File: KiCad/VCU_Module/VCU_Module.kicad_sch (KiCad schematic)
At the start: 5 parts, among them J1 5810132011, J5 pin header, J7 5V, J8 3V3, J9 GND

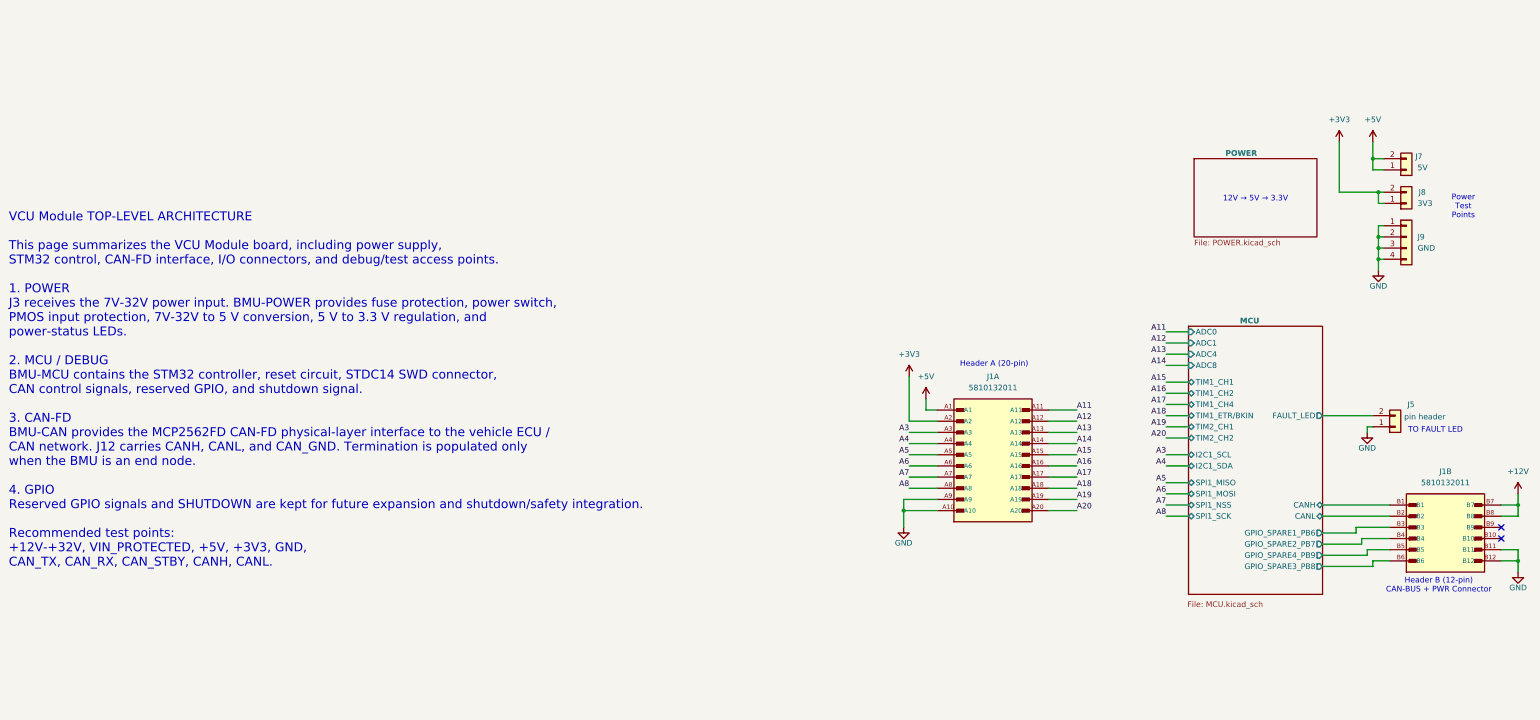
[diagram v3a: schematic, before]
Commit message: adding 'devkit' headers to make connections sustomizable inside of the enclosure
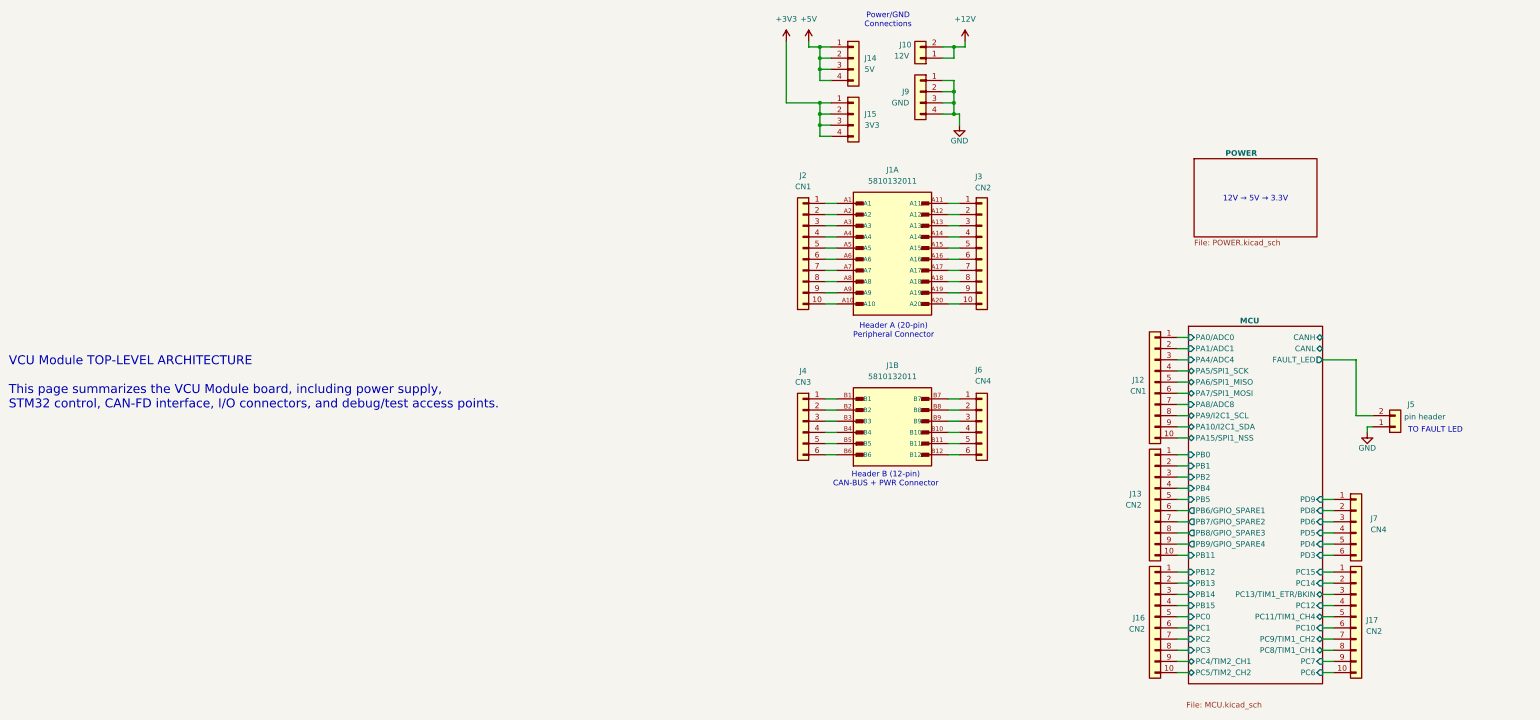
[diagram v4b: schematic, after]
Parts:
- removed J7: 5V, Connector_PinHeader_2.54mm:PinHeader_1x02_P2.54mm_Vertical, symbol Connector_Generic:Conn_01x02
- removed J8: 3V3, Connector_PinHeader_2.54mm:PinHeader_1x02_P2.54mm_Vertical, symbol Connector_Generic:Conn_01x02
- added J10: 12V, Connector_PinHeader_2.54mm:PinHeader_1x02_P2.54mm_Vertical, symbol Connector_Generic:Conn_01x02
- added J12, J2: CN1, symbol Connector_Generic:Conn_01x10
- added J13, J16, J17, J3: CN2, symbol Connector_Generic:Conn_01x10
- added J14: 5V, Connector_PinHeader_2.54mm:PinHeader_1x04_P2.54mm_Vertical, symbol Connector_Generic:Conn_01x04
- added J15: 3V3, Connector_PinHeader_2.54mm:PinHeader_1x04_P2.54mm_Vertical, symbol Connector_Generic:Conn_01x04
- added J4: CN3, symbol Connector_Generic:Conn_01x06
- added J6, J7: CN4, symbol Connector_Generic:Conn_01x06
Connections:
- net +12V: now also J10.1 (Pin_1), J10.2 (Pin_2); no longer J1.B7, J1.B8
- net +3V3: now also J15.1 (Pin_1), J15.2 (Pin_2), J15.3 (Pin_3), J15.4 (Pin_4); no longer J1.A2
- net +5V: now also J14.1 (Pin_1), J14.2 (Pin_2), J14.3 (Pin_3), J14.4 (Pin_4); no longer J1.A1
- net GND: no longer J1.A10, J1.A9, J1.B11, J1.B12
- net MCU/CANH: no longer J1.B1
- net MCU/CANL: no longer J1.B2
- net at J1.B10: now also J6.4 (Pin_4)
- net at J1.B9: now also J6.3 (Pin_3)
- net A11: no longer names the net of J1.A11
- net A11: now also J3.1 (Pin_1)
- net A12: no longer names the net of J1.A12
- net A12: now also J3.2 (Pin_2)
- net A13: no longer names the net of J1.A13
- net A13: now also J3.3 (Pin_3)
- net A14: no longer names the net of J1.A14
- net A14: now also J3.4 (Pin_4)
- net A15: no longer names the net of J1.A15
- net A15: now also J3.5 (Pin_5)
- net A16: no longer names the net of J1.A16
- net A16: now also J3.6 (Pin_6)
- net A17: no longer names the net of J1.A17
- net A17: now also J3.7 (Pin_7)
- net A18: no longer names the net of J1.A18
- net A18: now also J3.8 (Pin_8)
- net A19: no longer names the net of J1.A19
- net A19: now also J3.9 (Pin_9)
- net A20: no longer names the net of J1.A20
- net A20: now also J3.10 (Pin_10)
- net A3: no longer names the net of J1.A3
- net A3: now also J2.3 (Pin_3)
- net A4: no longer names the net of J1.A4
- net A4: now also J2.4 (Pin_4)
- net A5: no longer names the net of J1.A5
- net A5: now also J2.5 (Pin_5)
- net A6: no longer names the net of J1.A6
- net A6: now also J2.6 (Pin_6)
- net A7: no longer names the net of J1.A7
- net A7: now also J2.7 (Pin_7)
- net A8: no longer names the net of J1.A8
- net A8: now also J2.8 (Pin_8)
- net MCU/GPIO_SPARE1_PB6: no longer names the net of J1.B3
- net MCU/GPIO_SPARE1_PB6: now also J4.3 (Pin_3)
- net MCU/GPIO_SPARE2_PB7: no longer names the net of J1.B4
- net MCU/GPIO_SPARE2_PB7: now also J4.4 (Pin_4)
- net MCU/GPIO_SPARE3_PB8: no longer names the net of J1.B6
- net MCU/GPIO_SPARE3_PB8: now also J4.6 (Pin_6)
- net MCU/GPIO_SPARE4_PB9: no longer names the net of J1.B5
- net MCU/GPIO_SPARE4_PB9: now also J4.5 (Pin_5)
- new net: J1.B7, J6.1 (Pin_1)
- new net: J1.B8, J6.2 (Pin_2)
- new net: J1.B11, J6.5 (Pin_5)
- new net: J1.B12, J6.6 (Pin_6)
- new net: J1.A1, J2.1 (Pin_1)
- new net: J1.A10, J2.10 (Pin_10)
- new net: J1.A2, J2.2 (Pin_2)
- new net: J1.A9, J2.9 (Pin_9)
- new net: J1.B1, J4.1 (Pin_1)
- new net: J1.B2, J4.2 (Pin_2)
- new net MCU/PA0/ADC0: J12.1 (Pin_1)
- new net MCU/PA10/I2C1_SDA: J12.9 (Pin_9)
- new net MCU/PA15/SPI1_NSS: J12.10 (Pin_10)
- new net MCU/PA1/ADC1: J12.2 (Pin_2)
- new net MCU/PA4/ADC4: J12.3 (Pin_3)
- new net MCU/PA5/SPI1_SCK: J12.4 (Pin_4)
- new net MCU/PA6/SPI1_MISO: J12.5 (Pin_5)
- new net MCU/PA7/SPI1_MOSI: J12.6 (Pin_6)
- new net MCU/PA8/ADC8: J12.7 (Pin_7)
- new net MCU/PA9/I2C1_SCL: J12.8 (Pin_8)
- new net MCU/PB0: J13.1 (Pin_1)
- new net MCU/PB1: J13.2 (Pin_2)
- new net MCU/PB11: J13.10 (Pin_10)
- new net MCU/PB12: J16.1 (Pin_1)
- new net MCU/PB13: J16.2 (Pin_2)
- new net MCU/PB14: J16.3 (Pin_3)
- new net MCU/PB15: J16.4 (Pin_4)
- new net MCU/PB2: J13.3 (Pin_3)
- new net MCU/PB4: J13.4 (Pin_4)
- new net MCU/PB5: J13.5 (Pin_5)
- new net MCU/PB6/GPIO_SPARE1: J13.6 (Pin_6)
- new net MCU/PB7/GPIO_SPARE2: J13.7 (Pin_7)
- new net MCU/PB8/GPIO_SPARE3: J13.8 (Pin_8)
- new net MCU/PB9/GPIO_SPARE4: J13.9 (Pin_9)
- new net MCU/PC0: J16.5 (Pin_5)
- new net MCU/PC1: J16.6 (Pin_6)
- new net MCU/PC10: J17.6 (Pin_6)
- new net MCU/PC11/TIM1_CH4: J17.5 (Pin_5)
- new net MCU/PC12: J17.4 (Pin_4)
- new net MCU/PC13/TIM1_ETR/BKIN: J17.3 (Pin_3)
- new net MCU/PC14: J17.2 (Pin_2)
- new net MCU/PC15: J17.1 (Pin_1)
- new net MCU/PC2: J16.7 (Pin_7)
- new net MCU/PC3: J16.8 (Pin_8)
- new net MCU/PC4/TIM2_CH1: J16.9 (Pin_9)
- new net MCU/PC5/TIM2_CH2: J16.10 (Pin_10)
- new net MCU/PC6: J17.10 (Pin_10)
- new net MCU/PC7: J17.9 (Pin_9)
- new net MCU/PC8/TIM1_CH1: J17.8 (Pin_8)
- new net MCU/PC9/TIM1_CH2: J17.7 (Pin_7)
- new net MCU/PD3: J7.6 (Pin_6)
- new net MCU/PD4: J7.5 (Pin_5)
- new net MCU/PD5: J7.4 (Pin_4)
- new net MCU/PD6: J7.3 (Pin_3)
- new net MCU/PD8: J7.2 (Pin_2)
- new net MCU/PD9: J7.1 (Pin_1)
- no-connect marks 2 -> 0
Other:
- sheet MCU ports: added PA0/ADC0, PA10/I2C1_SDA, PA15/SPI1_NSS, PA1/ADC1, PA4/ADC4, PA5/SPI1_SCK, PA6/SPI1_MISO, PA7/SPI1_MOSI, PA8/ADC8, PA9/I2C1_SCL, PB0, PB1, PB11, PB12, PB13, PB14, PB15, PB2, PB4, PB5, PB6/GPIO_SPARE1, PB7/GPIO_SPARE2, PB8/GPIO_SPARE3, PB9/GPIO_SPARE4, PC0, PC1, PC10, PC11/TIM1_CH4, PC12, PC13/TIM1_ETR/BKIN, PC14, PC15, PC2, PC3, PC4/TIM2_CH1, PC5/TIM2_CH2, PC6, PC7, PC8/TIM1_CH1, PC9/TIM1_CH2, PD3, PD4, PD5, PD6, PD8, PD9; removed ADC0, ADC1, ADC4, ADC8, GPIO_SPARE1_PB6, GPIO_SPARE2_PB7, GPIO_SPARE3_PB8, GPIO_SPARE4_PB9, I2C1_SCL, I2C1_SDA, SPI1_MISO, SPI1_MOSI, SPI1_NSS, SPI1_SCK, TIM1_CH1, TIM1_CH2, TIM1_CH4, TIM1_ETR/BKIN, TIM2_CH1, TIM2_CH2
- note added: "Header A (20-pin) Peripheral Connector"
- note added: "Power/GND Connections"
- note added: "VCU Module TOP-LEVEL ARCHITECTURE This page summarizes the VCU Module board, including power supply, STM32 control, CAN-FD interface, I/O connectors, and debug/test access points."
- note removed: "Header A (20-pin)"
- note removed: "Power Test Points"
- note removed: "VCU Module TOP-LEVEL ARCHITECTURE This page summarizes the VCU Module board, including power supply, STM32 control, CAN-FD interface, I/O connectors, and debug/test access points. 1. POWER J3 receives the 7V-32V power input. BMU-POWER provides fuse protection, power switch, PMOS input protection, 7V-32V to 5 V conversion, 5 V to 3.3 V regulation, and power-status LEDs. 2. MCU / DEBUG BMU-MCU cont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"
- moved on the sheet: J1A, J1B

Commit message: added new power supply components, new power supply circuitry needs finishing
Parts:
- added C1, C2, C3: 10u, Capacitor_SMD:C_0805_2012Metric, symbol Device:C_Small
- added C4: 220n, Capacitor_SMD:C_0805_2012Metric, symbol Device:C_Small
- added CR1: MMSZ5245B-7-F, VMS_Footprints:SOD123_DIO, symbol MMSZ5245B_7_F:MMSZ5245B-7-F
- added D1, D2: GRN, LED_SMD:LED_0805_2012Metric_Pad1.15x1.40mm_HandSolder, symbol Device:LED
- added F1: Fuse, Fuse:Fuse_1206_3216Metric, symbol Device:Fuse
- added Q1: AO3401A, Package_TO_SOT_SMD:SOT-23, symbol Transistor_FET:AO3401A
- added R1, R4, R5: 100k, Resistor_SMD:R_0805_2012Metric, symbol Device:R_Small_US
- added R2, R3: 1k, Resistor_SMD:R_0805_2012Metric, symbol Device:R_Small_US
- added S1: 100SP1T1B4M2QE, VMS_Footprints:SW_100SP1T1B4M2QE, symbol 100SP1T1B4M2QE:100SP1T1B4M2QE
- added TP10, TP11, TP7, TP8, TP9: TestPoint_Small, TestPoint:TestPoint_THTPad_D1.5mm_Drill0.7mm, symbol Connector:TestPoint_Square
- added U1: OKI-78SR-5_1.5-W36-C, Converter_DCDC:Converter_DCDC_Murata_OKI-78SR_Vertical, symbol Converter_DCDC:OKI-78SR-5_1.5-W36-C
- added U2: TLV75533PDBV, Package_TO_SOT_SMD:SOT-23-5, symbol Regulator_Linear:TLV75533PDBV
- added U3: LMR33640DDDA, Package_SO:Texas_HSOP-8-1EP_3.9x4.9mm_P1.27mm_ThermalVias, symbol Regulator_Switching:LMR33640DDDA
- added U4: FDC6301N, FDC6301N:SSOT-6, symbol FDC6301N:FDC6301N
- J12: value CN1 -> MCU1
- J13: value CN2 -> MCU2
- J16: value CN2 -> MCU3
- J17: value CN2 -> MCU4
- J7: value CN4 -> MCU5
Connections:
- net +12V: now also F1.2, TP7.1
- net +3V3: now also C2.1, R3.2, R5.2, TP11.1, U2.5 (OUT)
- net +5V: now also C1.1, R2.2, R4.2, TP10.1, U1.3 (OUT), U2.1 (IN), U2.3 (EN)
- net GND: now also C1.2, C2.2, C3.2, C4.2, D1.1 (K), D2.1 (K), R1.2, TP9.1, U1.2 (GND), U2.2 (GND), U3.1 (GND), U3.9 (GND), U4.2, U4.6
- new net: CR1.2, Q1.1 (G), R1.1
- new net: Q1.3 (D), S1.1
- new net: D2.2 (A), R3.1
- new net: D1.2 (A), R2.1
- new net: F1.1, S1.2
- new net PG_3V3: R5.1, U3.4 (PG), U4.3
- new net PG_5V: R4.1, U4.5
- new net VDD: C3.1, C4.1, U3.2 (VIN), U3.3 (EN)
- new net VIN_PROTECTED: CR1.1, Q1.2 (S), TP8.1, U1.1 (IN)
- no-connect marks 0 -> 1
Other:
- removed sheet POWER
- note added: "3.3V @ 500 mA LDO"
- note added: "3V3 Supply Input Range: 3.8V-36V Output Range: 1V-24V"
- note added: "5V @ 1.5 A SPS"
- note added: "D"
- note added: "Enclosure Header A (20-pin) Peripheral Connector"
- note added: "Enclosure Header B (12-pin) CAN-BUS + PWR Connector"
- note added: "G"
- note added: "Main power input from bus connector 3.8V-36V"
- note added: "PCB/Enclosure Output Connectors"
- note added: "Protection"
- note added: "S"
- note added: "use a tps series switching power supply, at least 30V MHz class of switching frequencies, internal fets, sychronous rectification, do two of these, 1 for 5v and 1 for 3.3v, package with leads"
- note removed: "12V → 5V → 3.3V"
- note removed: "Header A (20-pin) Peripheral Connector"
- note removed: "Header B (12-pin) CAN-BUS + PWR Connector"
- moved on the sheet: J10, J12, J13, J14, J15, J16, J17, J1A, J1B, J2, J3, J4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

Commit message: finished reworking power supply with new LMR regulators, reorganized schematic, added description to top page, added user leds with identical layout to the nucleo c092 schematic
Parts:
- removed C1, C2: 10u, Capacitor_SMD:C_0805_2012Metric, symbol Device:C_Small
- removed D2: GRN, LED_SMD:LED_0805_2012Metric_Pad1.15x1.40mm_HandSolder, symbol Device:LED
- removed R3: 1k, Resistor_SMD:R_0805_2012Metric, symbol Device:R_Small_US
- removed TP10, TP11, TP7, TP8, TP9: TestPoint_Small, TestPoint:TestPoint_THTPad_D1.5mm_Drill0.7mm, symbol Connector:TestPoint_Square
- removed U1: OKI-78SR-5_1.5-W36-C, Converter_DCDC:Converter_DCDC_Murata_OKI-78SR_Vertical, symbol Converter_DCDC:OKI-78SR-5_1.5-W36-C
- removed U2: TLV75533PDBV, Package_TO_SOT_SMD:SOT-23-5, symbol Regulator_Linear:TLV75533PDBV
- removed U4: FDC6301N, FDC6301N:SSOT-6, symbol FDC6301N:FDC6301N
- added C10: 10u, Capacitor_SMD:C_0805_2012Metric, symbol Device:C_Small
- added C11: 220n, Capacitor_SMD:C_0805_2012Metric, symbol Device:C_Small
- added C12, C9: 1u, Capacitor_SMD:C_0805_2012Metric, symbol Device:C_Small
- added C18, C5: 0.1u, Capacitor_SMD:C_0805_2012Metric, symbol Device:C_Small
- added C19, C20, C21, C6, C7, C8: 22u, Capacitor_SMD:C_0805_2012Metric, symbol Device:C_Small
- added D4: GRN, LED_SMD:LED_0805_2012Metric_Pad1.15x1.40mm_HandSolder, symbol Device:LED
- added L1, L2: 3.3u, symbol Device:L
- added R6: 100k, Resistor_SMD:R_0805_2012Metric, symbol Device:R_Small_US
- added R7: 43.2k, Resistor_SMD:R_0805_2012Metric, symbol Device:R_Small_US
- added R8: 1k, Resistor_SMD:R_0805_2012Metric, symbol Device:R_Small_US
- added U4: LMR33640DDDA, Package_SO:Texas_HSOP-8-1EP_3.9x4.9mm_P1.27mm_ThermalVias, symbol Regulator_Switching:LMR33640DDDA
- R5: value 100k -> 43.2k
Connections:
- net PG_5V is gone; now on an unnamed net: R4.1
- net +12V: no longer F1.2
- net +3V3: now also R2.2, R4.2, C6.1, C7.1, C8.1, L1.2; no longer R5.2
- net +5V: now also C19.1, C20.1, C21.1, L2.2, R6.2, R8.2; no longer R2.2, R4.2
- net GND: now also R5.1, C10.2, C11.2, C12.2, C19.2, C20.2, C21.2, C6.2, C7.2, C8.2, C9.2, D4.1 (K), R7.1, U4.1 (GND), U4.9 (GND)
- net VDD: now also F1.2; no longer C3.1, C4.1, U3.2 (VIN), U3.3 (EN)
- net VIN_PROTECTED: now also C3.1, C4.1, U3.2 (VIN), U3.3 (EN), C10.1, C11.1, U4.2 (VIN), U4.3 (EN)
- net at U3.5 (FB): now also R5.2
- net at U3.6 (VCC): now also C9.1
- net at U3.7 (BOOT): now also C5.2
- net at U3.8 (SW): now also C5.1, L1.1
- net PG_3V3: no longer names the net of U3.4 (PG)
- net PG_3V3: no longer R5.1
- new net: R6.1, R7.2, U4.5 (FB)
- new net: C12.1, U4.6 (VCC)
- new net: C18.2, U4.7 (BOOT)
- new net: C18.1, L2.1, U4.8 (SW)
- new net: D4.2 (A), R8.1
- no-connect marks 1 -> 3
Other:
- note added: "3V3 Supply Input Range: 3.8V-36V"
- note added: "5V Supply Input Range: 3.8V-36V"
- note added: "MCU"
- note added: "VCU Module TOP-LEVEL ARCHITECTURE The "VMS VCU Dev Board" is the first iteration of the VCU module using a custom PCB designed to fit in a Cinch 2.25" x 3.35" enclosure The board accepts up to a 36V DC power source (needs to be manually connected from bus connector) and contains both 3.3V and 5V regulators to power the MCU and any external sensors/components The Cinch enclosure header consists of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"
- note added: "Voltage Regulators"
- note removed: "3.3V @ 500 mA LDO"
- note removed: "3V3 Supply Input Range: 3.8V-36V Output Range: 1V-24V"
- note removed: "5V @ 1.5 A SPS"
- note removed: "VCU Module TOP-LEVEL ARCHITECTURE This page summarizes the VCU Module board, including power supply, STM32 control, CAN-FD interface, I/O connectors, and debug/test access points."
- note removed: "use a tps series switching power supply, at least 30V MHz class of switching frequencies, internal fets, sychronous rectification, do two of these, 1 for 5v and 1 for 3.3v, package with leads"
- title: VEHICLE CONTROL UNIT (VCU) MODULE -> VEHICLE CONTROL UNIT (VCU) Dev Board
- moved on the sheet: C3, C4, J10, J12, J13, J14, J15, J16, J17, J5, J7, J9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

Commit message: fixed all socket header connections, placed and routed every component on PCB, added all 3d models to footprints
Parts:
- removed J13: MCU2, symbol Connector_Generic:Conn_01x10
- removed J16: MCU3, symbol Connector_Generic:Conn_01x10
- removed J17: MCU4, symbol Connector_Generic:Conn_01x10
- removed J5: pin header, Connector_PinHeader_2.54mm:PinHeader_1x02_P2.54mm_Vertical, symbol Connector_Generic:Conn_01x02
- removed J7: MCU5, symbol Connector_Generic:Conn_01x06
- added J13: MCU2, VMS_Footprints:1x10_Header_f, symbol Connector:Conn_01x10_Socket
- added J16: MCU3, VMS_Footprints:1x10_Header_f, symbol Connector:Conn_01x10_Socket
- added J17: MCU4, VMS_Footprints:1x10_Header_f, symbol Connector:Conn_01x10_Socket
- added J5: MCU6, Connector_PinHeader_2.54mm:PinHeader_1x04_P2.54mm_Vertical, symbol Connector:Conn_01x04_Socket
- added J7: MCU5, Connector_PinHeader_2.54mm:PinHeader_1x06_P2.54mm_Vertical, symbol Connector:Conn_01x06_Socket
- J10: symbol Connector_Generic:Conn_01x02 -> Connector:Conn_01x02_Socket
- J12, J2, J3: footprint (none) -> VMS_Footprints:1x10_Header_f; symbol Connector_Generic:Conn_01x10 -> Connector:Conn_01x10_Socket
- J14, J15, J9: symbol Connector_Generic:Conn_01x04 -> Connector:Conn_01x04_Socket
- J4, J6: footprint (none) -> Connector_PinHeader_2.54mm:PinHeader_1x06_P2.54mm_Vertical; symbol Connector_Generic:Conn_01x06 -> Connector:Conn_01x06_Socket
- L1, L2: footprint (none) -> Inductor_SMD:L_0805_2012Metric_Pad1.05x1.20mm_HandSolder
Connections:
- net +12V is gone; now on net VDD: J10.1 (Pin_1), J10.2 (Pin_2)
- net MCU/CANH: now also J5.1 (Pin_1), J5.2 (Pin_2)
- net MCU/CANL: now also J5.3 (Pin_3), J5.4 (Pin_4)
- net MCU/PA0/ADC0: now also J13.1 (Pin_1); no longer J12.1 (Pin_1)
- net MCU/PA10/I2C1_SDA: now also J17.3 (Pin_3); no longer J12.9 (Pin_9)
- net MCU/PA15/SPI1_NSS: now also J17.4 (Pin_4); no longer J12.10 (Pin_10)
- net MCU/PA1/ADC1: now also J13.2 (Pin_2); no longer J12.2 (Pin_2)
- net MCU/PA4/ADC4: now also J13.3 (Pin_3); no longer J12.3 (Pin_3)
- net MCU/PA5/SPI1_SCK: now also J13.4 (Pin_4); no longer J12.4 (Pin_4)
- net MCU/PA6/SPI1_MISO: now also J13.5 (Pin_5); no longer J12.5 (Pin_5)
- net MCU/PA7/SPI1_MOSI: now also J13.6 (Pin_6); no longer J12.6 (Pin_6)
- net MCU/PA8/ADC8: now also J16.7 (Pin_7); no longer J12.7 (Pin_7)
- net MCU/PA9/I2C1_SCL: now also J16.8 (Pin_8); no longer J12.8 (Pin_8)
- net MCU/PB0: now also J13.9 (Pin_9)
- net MCU/PB1: now also J13.10 (Pin_10)
- net MCU/PB11: now also J16.2 (Pin_2)
- net MCU/PB12: now also J16.3 (Pin_3)
- net MCU/PB13: now also J16.4 (Pin_4)
- net MCU/PB14: now also J16.5 (Pin_5)
- net MCU/PB15: now also J16.6 (Pin_6)
- net MCU/PB2: now also J16.1 (Pin_1)
- net MCU/PB4: now also J7.1 (Pin_1)
- net MCU/PB5: now also J7.2 (Pin_2)
- net MCU/PB6/GPIO_SPARE1: now also J7.3 (Pin_3)
- net MCU/PB7/GPIO_SPARE2: now also J7.4 (Pin_4)
- net MCU/PB8/GPIO_SPARE3: now also J7.5 (Pin_5)
- net MCU/PB9/GPIO_SPARE4: now also J7.6 (Pin_6)
- net MCU/PC0: now also J12.7 (Pin_7)
- net MCU/PC1: now also J12.8 (Pin_8)
- net MCU/PC10: now also J12.1 (Pin_1)
- net MCU/PC11/TIM1_CH4: now also J12.2 (Pin_2)
- net MCU/PC12: now also J12.3 (Pin_3)
- net MCU/PC13/TIM1_ETR/BKIN: now also J12.4 (Pin_4)
- net MCU/PC14: now also J12.5 (Pin_5)
- net MCU/PC15: now also J12.6 (Pin_6)
- net MCU/PC2: now also J12.9 (Pin_9)
- net MCU/PC3: now also J12.10 (Pin_10)
- net MCU/PC4/TIM2_CH1: now also J13.7 (Pin_7)
- net MCU/PC5/TIM2_CH2: now also J13.8 (Pin_8)
- net MCU/PC6: now also J16.9 (Pin_9)
- net MCU/PC7: now also J16.10 (Pin_10)
- net MCU/PC8/TIM1_CH1: now also J17.5 (Pin_5)
- net MCU/PC9/TIM1_CH2: now also J17.6 (Pin_6)
- net MCU/PD3: now also J17.7 (Pin_7)
- net MCU/PD4: now also J17.8 (Pin_8)
- net MCU/PD5: now also J17.9 (Pin_9)
- net MCU/PD6: now also J17.10 (Pin_10)
- net MCU/PD8: now also J17.1 (Pin_1)
- net MCU/PD9: now also J17.2 (Pin_2)
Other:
- sheet MCU ports: added none; removed FAULT_LED
- note removed: "TO FAULT LED"
- moved on the sheet: J10
